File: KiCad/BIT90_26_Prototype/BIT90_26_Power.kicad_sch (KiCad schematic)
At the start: 41 parts, among them J10 +5V In (2.1mm), J8 Mean Well GP25A13A-R1B, J9 +5V In (USB), SW67 ON/OFF, U10 74LS04, U12 74LS00, U14 74LS05, U15 74LS107, U25 LM393, U7 74LS74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

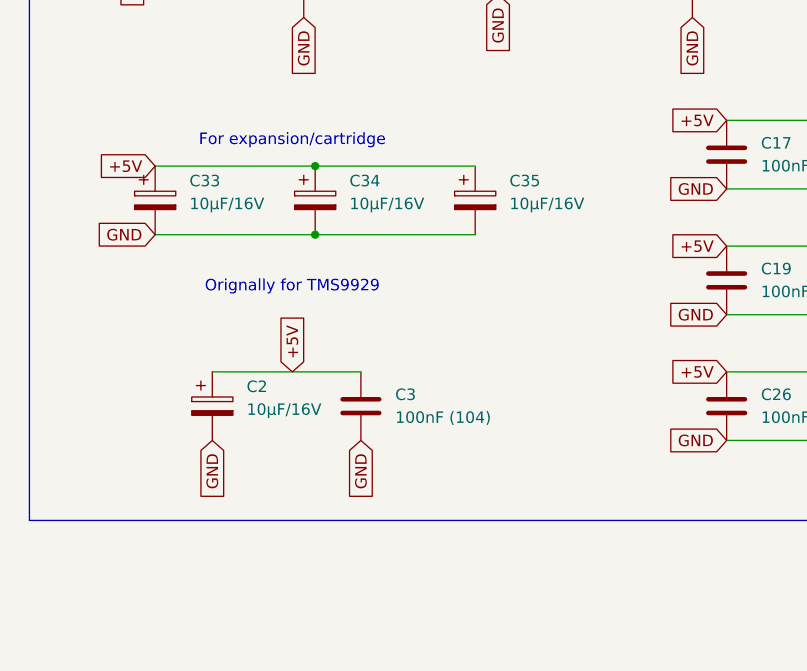
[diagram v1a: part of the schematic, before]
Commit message: Added more signal analysis to schematic
Would be nice to reduce the amount of glue logic
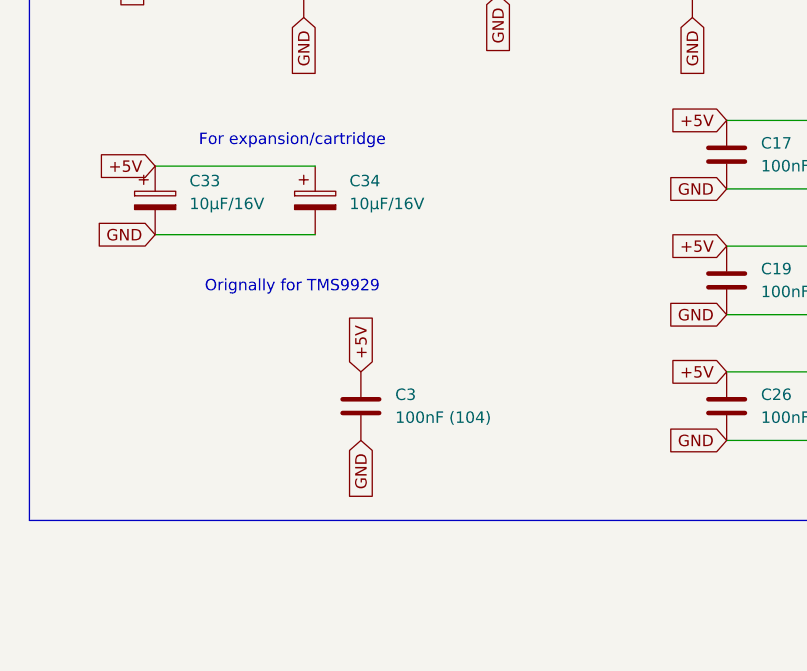
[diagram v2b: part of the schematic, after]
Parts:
- removed C2, C35: 10µF/16V, Capacitor_THT:CP_Radial_D6.3mm_P2.50mm, symbol Device:C_Polarized
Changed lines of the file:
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@@
 	)
 	(junction
-		(at 48.26 72.39)
-		(diameter 0)
-		(color 0 0 0 0)
-	)
-	(junction
 		(at 152.4 102.87)
 		(diameter 0)
@@
 	)
 	(junction
-		(at 48.26 80.01)
-		(diameter 0)
-		(color 0 0 0 0)
-	)
-	(junction
 		(at 190.5 102.87)
 		(diameter 0)
@@
 	(wire
 		(pts
-			(xy 48.26 72.39) (xy 66.04 72.39)
-		)
-		(stroke
-			(width 0)
-			(type default)
-		)
-	)
-	(wire
-		(pts
 			(xy 93.98 88.9) (xy 113.03 88.9)
 		)
@@
 	(wire
 		(pts
-			(xy 48.26 80.01) (xy 66.04 80.01)
-		)
-		(stroke
-			(width 0)
-			(type default)
-		)
-	)
-	(wire
-		(pts
 			(xy 133.35 81.28) (xy 152.4 81.28)
 		)
@@
 	(wire
 		(pts
-			(xy 36.83 95.25) (xy 53.34 95.25)
-		)
-		(stroke
-			(width 0)
-			(type default)
-		)
-	)
-	(wire
-		(pts
 			(xy 190.5 102.87) (xy 209.55 102.87)
 		)
@@
 	(global_label "GND"
 		(shape input)
-		(at 36.83 102.87 270)
-		(fields_autoplaced yes)
-		(effects
-			(font
-				(size 1.27 1.27)
-			)
-			(justify right)
-		)
-		(property "Intersheetrefs" "${INTERSHEET_REFS}"
-			(at 36.83 109.7257 90)
-			(effects
-				(font
-					(size 1.27 1.27)
-				)
-				(justify right)
-				(hide yes)
-			)
-		)
-	)
-	(global_label "GND"
-		(shape input)
 		(at 110.49 55.88 270)
 		(fields_autoplaced yes)
@@
 	(global_label "+5V"
 		(shape input)
-		(at 45.72 95.25 90)
+		(at 53.34 95.25 90)
 		(fields_autoplaced yes)
 		(effects
@@
 		)
 		(property "Intersheetrefs" "${INTERSHEET_REFS}"
-			(at 45.72 88.3943 90)
+			(at 53.34 88.3943 90)
 			(effects
 				(font
@@
 	(symbol
 		(lib_id "Device:C_Polarized")
-		(at 36.83 99.06 0)
-		(unit 1)
-		(exclude_from_sim no)
-		(in_bom yes)
-		(on_board yes)
-		(dnp no)
-		(fields_autoplaced yes)
-		(property "Reference" "C2"
-			(at 40.64 96.9009 0)
-			(effects
-				(font
-					(size 1.27 1.27)
-				)
-				(justify left)
-			)
-		)
-		(property "Value" "10µF/16V"
-			(at 40.64 99.4409 0)
-			(effects
-				(font
-					(size 1.27 1.27)
-				)
-				(justify left)
-			)
-		)
-		(property "Footprint" "Capacitor_THT:CP_Radial_D6.3mm_P2.50mm"
-			(at 37.7952 102.87 0)
-			(effects
-				(font
-					(size 1.27 1.27)
-				)
-				(hide yes)
-			)
-		)
-		(property "Datasheet" "~"
-			(at 36.83 99.06 0)
-			(effects
-				(font
-					(size 1.27 1.27)
-				)
-				(hide yes)
-			)
-		)
-		(property "Description" "Polarized capacitor"
-			(at 36.83 99.06 0)
-			(effects
-				(font
-					(size 1.27 1.27)
-				)
-				(hide yes)
-			)
-		)
-		(pin "2"
-		)
-		(pin "1"
-		)
-		(instances
-			(project "BIT90_26_Prototype"
-				(path "/d65498c3-6385-4920-ac0f-4c76daf90780/4eb1b27c-0de4-437c-bec4-8709ba05b3a7"
-					(reference "C2")
-					(unit 1)
-				)
-			)
-		)
-	)
-	(symbol
-		(lib_id "Device:C_Polarized")
 		(at 30.48 76.2 0)
 		(unit 1)
@@
 					(unit 1)
 				)
-			)
-		)
-	)
-	(symbol
-		(lib_id "Device:C_Polarized")
-		(at 66.04 76.2 0)
-		(unit 1)
-		(exclude_from_sim no)
-		(in_bom yes)
-		(on_board yes)
-		(dnp no)
-		(fields_autoplaced yes)
-		(property "Reference" "C35"
-			(at 69.85 74.0409 0)
-			(effects
-				(font
-					(size 1.27 1.27)
-				)
-				(justify left)
-			)
-		)
-		(property "Value" "10µF/16V"
-			(at 69.85 76.5809 0)
-			(effects
-				(font
-					(size 1.27 1.27)
-				)
-				(justify left)
-			)
-		)
-		(property "Footprint" "Capacitor_THT:CP_Radial_D6.3mm_P2.50mm"
-			(at 67.0052 80.01 0)
-			(effects
-				(font
-					(size 1.27 1.27)
-				)
-				(hide yes)
-			)
-		)
-		(property "Datasheet" "~"
-			(at 66.04 76.2 0)
-			(effects
-				(font
-					(size 1.27 1.27)
-				)
-				(hide yes)
-			)
-		)
-		(property "Description" "Polarized capacitor"
-			(at 66.04 76.2 0)
-			(effects
-				(font
-					(size 1.27 1.27)
-				)
-				(hide yes)
-			)
-		)
-		(pin "1"
-		)
-		(pin "2"
-		)
-		(instances
-			(project "BIT90_26_Prototype"
-				(path "/d65498c3-6385-4920-ac0f-4c76daf90780/4eb1b27c-0de4-437c-bec4-8709ba05b3a7"
-					(reference "C35")
-					(unit 1)
-				)
